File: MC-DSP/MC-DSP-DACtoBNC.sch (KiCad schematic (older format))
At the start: 18 parts, among them J80 5-1634513-1, J81 5-1634513-1, J82 5-1634513-1, U80 OPA365xxD, U81 OPA365xxD, U82 OPA365xxD

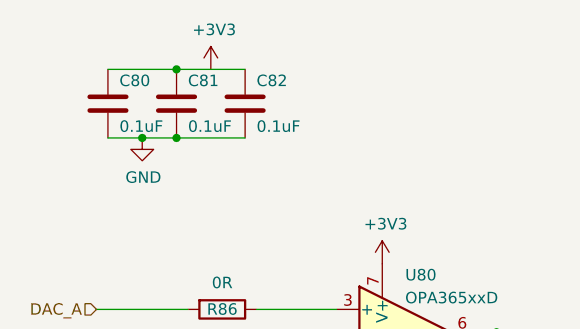
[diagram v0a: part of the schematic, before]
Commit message: Routed Last 11 tracks, fixed cu.4 gnd pour
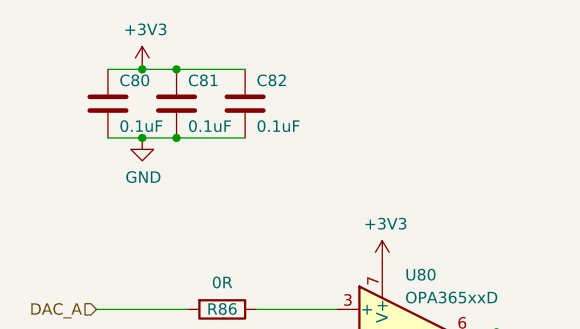
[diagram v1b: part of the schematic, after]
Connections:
- net +3V3: now also C80.2, C81.2, C82.2
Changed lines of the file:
@@
-	1    0    0    -1
-$EndComp
-$Comp
-L power:+3V3 #PWR?
-U 1 1 6243256E
-P 5100 1800
-AR Path="/6187F723/6243256E" Ref="#PWR?"  Part="1"
-AR Path="/61B9C0F2/6243256E" Ref="#PWR0142"  Part="1"
-F 0 "#PWR0142" H 5100 1650 50  0001 C CNN
-F 1 "+3V3" H 5115 1973 50  0000 C CNN
-F 2 "" H 5100 1800 50  0001 C CNN
-F 3 "" H 5100 1800 50  0001 C CNN
-	1    5100 1800
 	1    0    0    -1
 $EndComp
 Wire Wire Line
-	4650 1800 4950 1800
+	4650 1800 4800 1800
+$Comp
+L power:+3V3 #PWR?
+U 1 1 624C4B85
+P 4800 1800
+AR Path="/6187F723/624C4B85" Ref="#PWR?"  Part="1"
+AR Path="/61B9C0F2/624C4B85" Ref="#PWR?"  Part="1"
+F 0 "#PWR?" H 4800 1650 50  0001 C CNN
+F 1 "+3V3" H 4815 1973 50  0000 C CNN
+F 2 "" H 4800 1800 50  0001 C CNN
+F 3 "" H 4800 1800 50  0001 C CNN
+	1    4800 1800
+	1    0    0    -1
+$EndComp
+Connection ~ 4800 1800
+Wire Wire Line
+	4800 1800 4950 1800
 $EndSCHEMATC
